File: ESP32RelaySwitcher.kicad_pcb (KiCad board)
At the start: 2 copper layers, 152 x 64.5 mm, 103 parts, among them J1 POWER_IN, J10 BUTTON_1, J11 BUTTON_2, J12 BUTTON_3, J13 BUTTON_4, J14 BUTTON_5, J15 BUTTON_6, J16 BUTTON_7, J17 BUTTON_8, J18 SERIAL+GPIO, J2 RELAY_1, J3 RELAY_2, J4 RELAY_4, J5 RELAY_3, J6 RELAY_5, J7 RELAY_6, J8 RELAY_8, J9 RELAY_7, K1 G6E-134P-US DC5, K2 G6E-134P-US DC5, K3 G6E-134P-US DC5, K4 G6E-134P-US DC5, K5 G6E-134P-US DC5, K6 G6E-134P-US DC5, K7 G6E-134P-US DC5, K8 G6E-134P-US DC5, Q1 2N7002, Q2 2N7002, Q3 2N7002, Q4 2N7002, Q5 2N7002, Q6 2N7002, Q7 2N7002, Q8 2N7002, SW1 POWER, SW2 RESET, SW3 IO0, U1 LMR36520ADDAR, U2 AP1117-33, U3 DHT22, U4 ESP32-WROOM-32D, U5 TSOP382xx

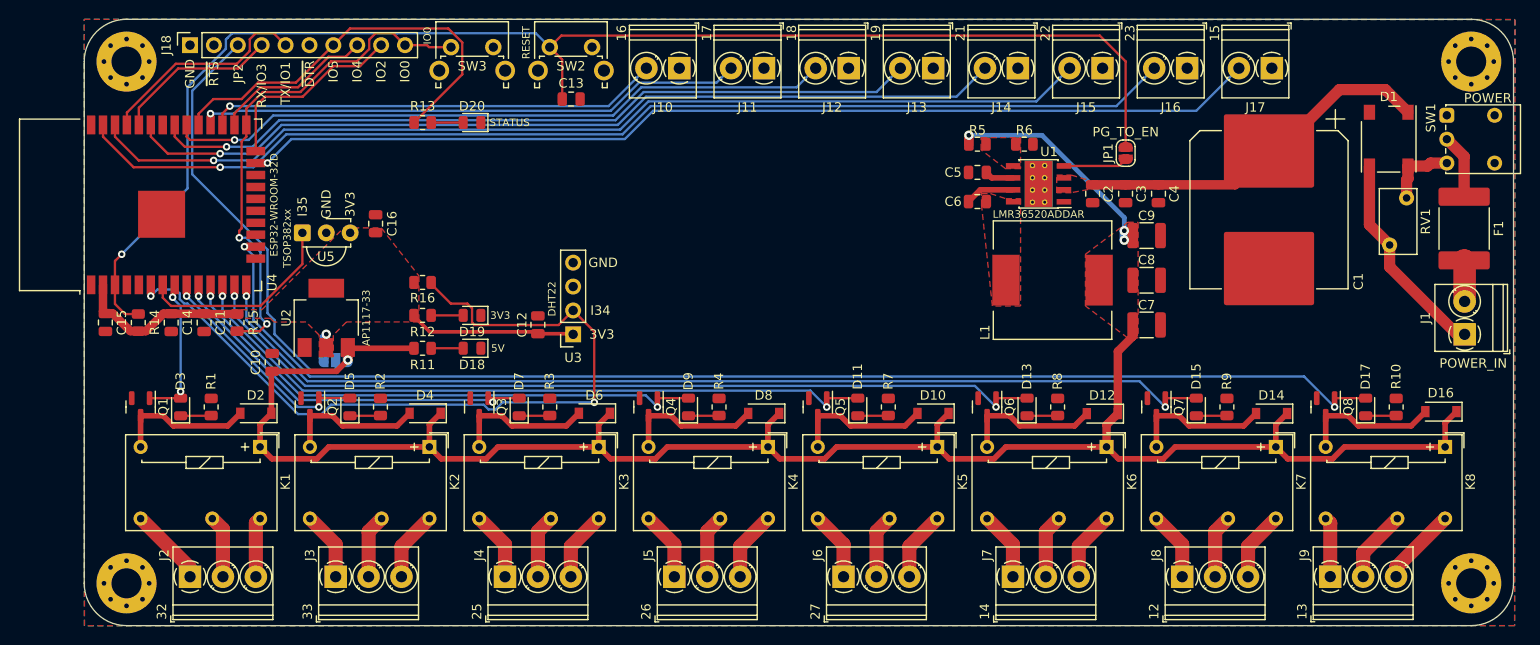
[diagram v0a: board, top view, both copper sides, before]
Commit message: Use parts I can actually get...
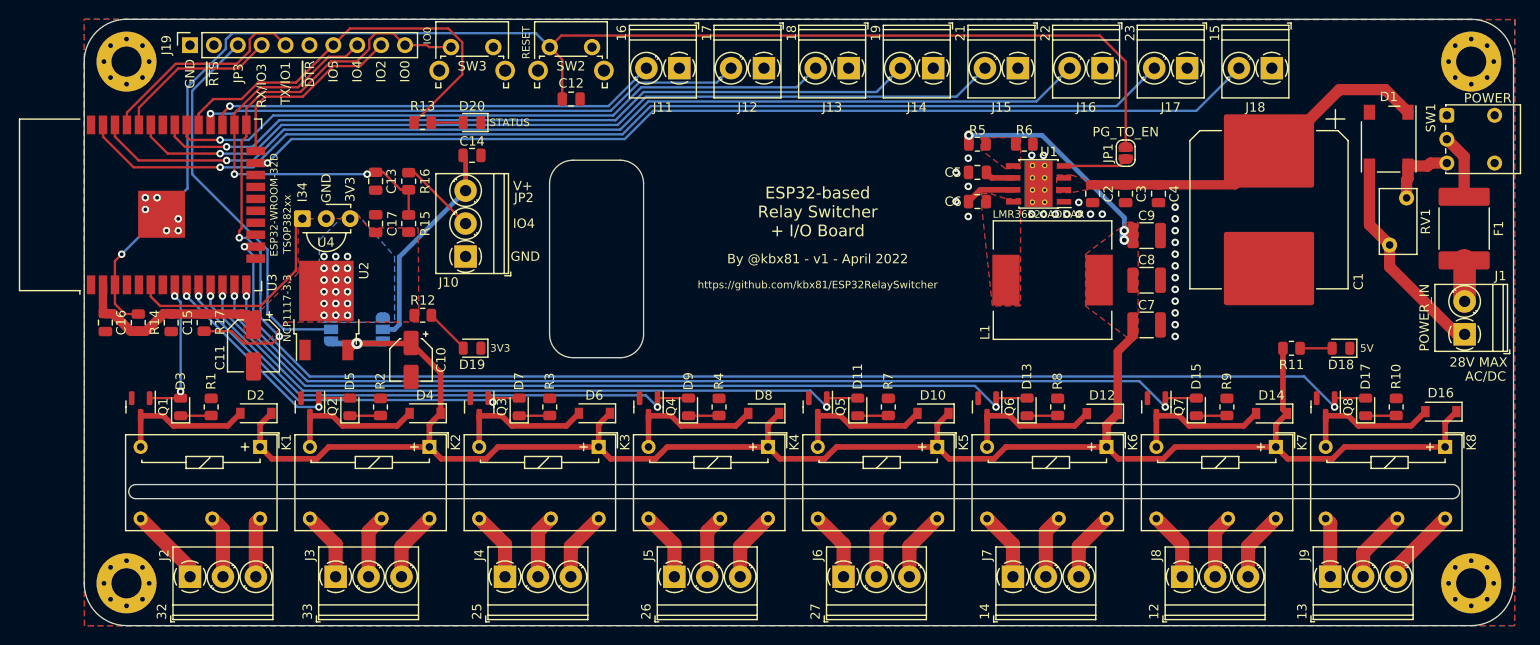
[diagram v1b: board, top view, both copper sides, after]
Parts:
- removed the C14 at (77.3, 92.8)
- removed the C15 at (70.3, 92.8)
- removed the U3 at (120.0, 94.0)
- added C11: 100 uF, Capacitor_SMD:CP_Elec_5x5.4, F.Cu at (86.0, 95.2)
- added C13: 470 pF, Capacitor_SMD:C_0805_2012Metric, F.Cu at (99.0, 77.7)
- added C16: 100 nF, Capacitor_SMD:C_0805_2012Metric, F.Cu at (70.3, 92.8)
- added J10: DS18B20, TerminalBlock_Phoenix:TerminalBlock_Phoenix_PT-1,5-3-3.5-H_1x03_P3.50mm_Horizontal, F.Cu at (108.6, 85.7)
- added JP2: J10_V_SEL, Jumper:SolderJumper-3_P1.3mm_Open_RoundedPad1.0x1.5mm, B.Cu at (99.8, 93.5)
- added R16: 0, Resistor_SMD:R_0805_2012Metric, F.Cu at (102.5, 77.7)
- C10: footprint Capacitor_SMD:C_0805_2012Metric -> Capacitor_SMD:CP_Elec_4x5.8
- JP3: renamed from JP2; value J18_V_SEL -> J19_V_SEL
- R15: renamed from R16; value 10K -> 4K7
- U2: value AP1117-33 -> NCP1117-3.3; footprint Package_TO_SOT_SMD:SOT-223-3_TabPin2 -> Package_TO_SOT_SMD:TO-252-2
- moved D18 92.4 mm to (201.6, 95.5)
- moved R11 92.4 mm to (196.4, 95.5)
- moved C14 19.3 mm to (109.2, 75.0), turned to 0 degrees
- moved C10 14.8 mm to (102.8, 96.7)
- moved R15 6.43 mm to (102.5, 82.2), turned to 90 degrees
- moved C15 3.50 mm to (77.3, 92.8), turned to -90 degrees
- moved R17 3.50 mm to (80.8, 92.8)
- moved D19 3.49 mm to (109.2, 95.5)
- moved JP3 3.30 mm to (94.3, 93.5), turned to 90 degrees
- moved U4 1.51 mm to (91.2, 81.7)
- moved U2 0.78 mm to (93.8, 91.5)
- renumbered C13 to C12, C12 to C14, C11 to C15, C16 to C17, J10 to J11, J11 to J12, J12 to J13, J13 to J14, J14 to J15, J15 to J16, J16 to J17, J17 to J18, J18 to J19, R15 to R17, U4 to U3, U5 to U4
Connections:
- C10 pad 1: GND -> +5V
- C10 pad 2: +5V -> GND
- C14 pad 1: +3V3 -> Net-(C14-Pad1)
- C15 pad 1: GND -> +3V3
- C15 pad 2: +3V3 -> GND
- R15 pad 1: /GPI34 -> +3V3
- R15 pad 2: +3V3 -> /GPIO4
- U4 pad 1: /GPI35 -> /GPI34
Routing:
- net /GPI34: track 84.7 -> 24.4 mm, vias 2 -> 0
- net /GPIO4: track 17.3 -> 43.6 mm, vias 0 -> 2
- net Net-(C14-Pad1): track 0.00 -> 23.0 mm
- net /GPI35: track 21.7 -> 0.00 mm
- net +3V3: track 40.8 -> 21.0 mm, vias 1 -> 18
- net Net-(J10-Pad2): track 0.00 -> 8.29 mm
- net /GPIO0: track 54.6 -> 61.9 mm
- net +5V: track 221.0 -> 228.2 mm
- net Net-(J19-Pad3): track 45.6 -> 41.3 mm
- net Net-(D19-Pad2): track 3.41 -> 4.90 mm
- net /GPIO32: track 15.8 -> 14.4 mm
- net GND: vias 0 -> 33
- added copper zone on B.Cu, net +3V3
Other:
- outline, holes or cut-outs redrawn
- board text added: "By @kbx81 - v1 - April 2022"
- board text added: "ESP32-based Relay Switcher + I/O Board"
- board text added: "https://github.com/kbx81/ESP32RelaySwitcher"

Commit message: Finishing
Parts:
- added J19: 3V3, Connector_PinSocket_2.54mm:PinSocket_1x02_P2.54mm_Vertical, F.Cu at (104.8, 90.5)
- added J20: 5V, Connector_PinSocket_2.54mm:PinSocket_1x02_P2.54mm_Vertical, F.Cu at (181.8, 97.0)
- JP3: value J19_V_SEL -> J21_V_SEL
- moved R12 5.94 mm to (102.5, 86.2), turned to -90 degrees
- moved C16 0.26 mm to (99.0, 82.0)
- moved R15 0.25 mm to (102.5, 82.0)
- moved D16 0.20 mm to (212.3, 102.4)
- renumbered C17 to C16, C16 to C17, J19 to J21
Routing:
- net Net-(J2-Pad1): track 8.35 -> 16.7 mm
- net Net-(J9-Pad3): track 8.33 -> 16.7 mm
- net Net-(J9-Pad2): track 7.67 -> 15.3 mm
- net Net-(J6-Pad3): track 7.41 -> 14.8 mm
- net Net-(J3-Pad3): track 7.41 -> 14.8 mm
- net Net-(J4-Pad3): track 7.41 -> 14.8 mm
- net Net-(J5-Pad3): track 7.40 -> 14.8 mm
- net Net-(J8-Pad3): track 7.40 -> 14.8 mm
- net Net-(J7-Pad3): track 7.40 -> 14.8 mm
- net Net-(D19-Pad2): track 4.90 -> 12.3 mm
- net Net-(J7-Pad1): track 7.32 -> 14.6 mm
- net Net-(J8-Pad1): track 7.32 -> 14.6 mm
- net Net-(J5-Pad1): track 7.32 -> 14.6 mm
- net Net-(J4-Pad1): track 7.32 -> 14.6 mm
- net Net-(J6-Pad1): track 7.31 -> 14.6 mm
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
